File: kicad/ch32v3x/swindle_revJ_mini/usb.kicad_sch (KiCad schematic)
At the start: 8 parts, among them J4 USB, U2 LM1117-3.3

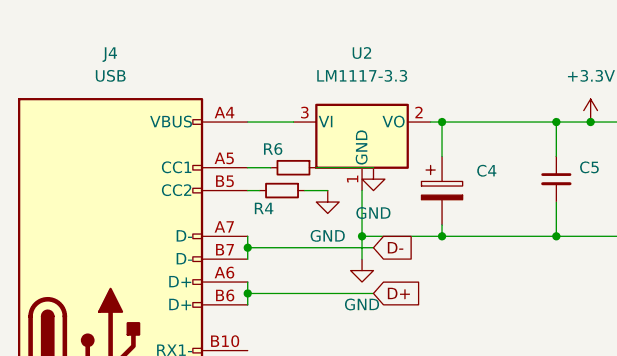
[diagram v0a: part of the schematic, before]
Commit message: add a WS2812b to the mini version, mini version for CH32,GD32 and RP2xxx
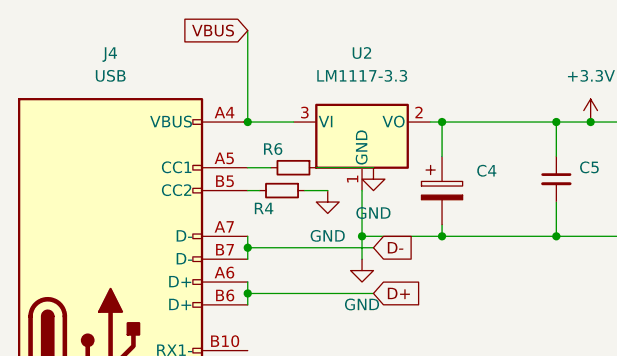
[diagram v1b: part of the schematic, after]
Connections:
- net VBUS: now reaches J4.A4 (VBUS), J4.A9 (VBUS), J4.B4 (VBUS), J4.B9 (VBUS), U2.3 (VI)
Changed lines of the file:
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@@
+	)
+	(junction
+		(at 101.6 45.72)
+		(diameter 0)
+		(color 0 0 0 0)
 	)
 	(junction
@@
 		(pts
 			(xy 123.19 57.15) (xy 123.19 58.42)
+		)
+		(stroke
+			(width 0)
+			(type default)
+		)
+	)
+	(wire
+		(pts
+			(xy 101.6 35.56) (xy 101.6 45.72)
 		)
 		(stroke
@@
 				(hide yes)
 			)
+		)
+	)
+	(global_label "VBUS"
+		(shape input)
+		(at 101.6 35.56 180)
+		(fields_autoplaced yes)
+		(effects
+			(font
+				(size 1.27 1.27)
+			)
+			(justify right)
+		)
+		(property "Intersheetrefs" "${INTERSHEET_REFS}"
+			(at 93.7162 35.56 0)
+			(effects
+				(font
+					(size 1.27 1.27)
+				)
+				(justify right)
+				(hide yes)
+			)

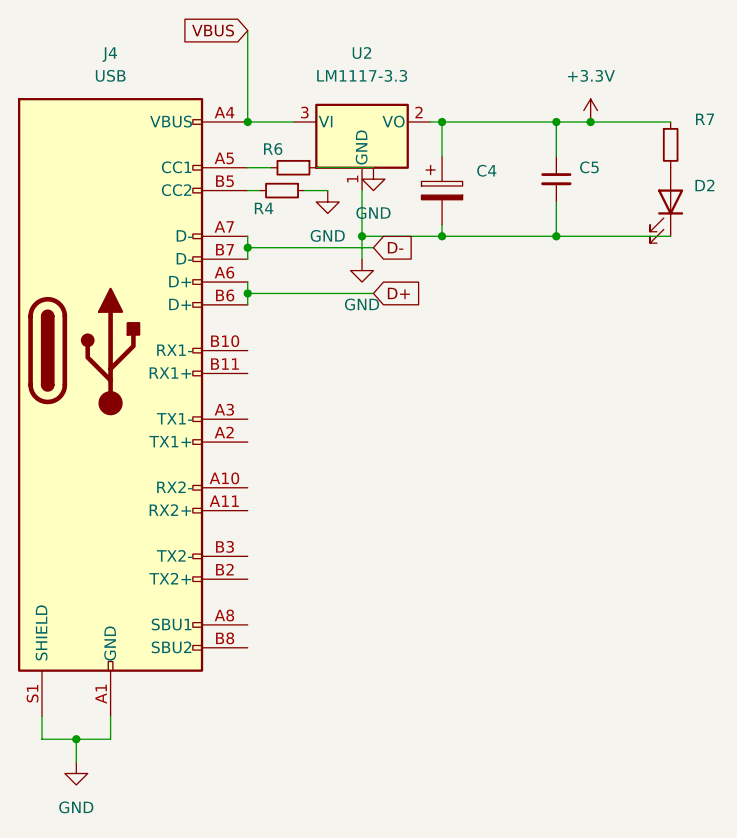
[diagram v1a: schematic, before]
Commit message: Kicad : ch32v3, add a (optional) 1.2k pullup on D+ so it can be used for GD32F303/64pins package
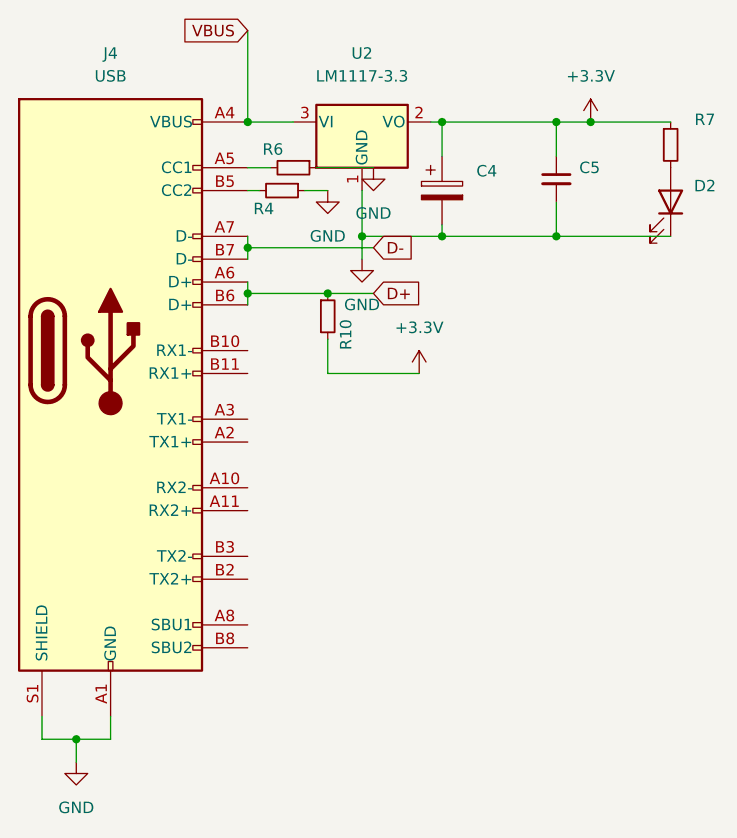
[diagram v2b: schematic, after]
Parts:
- added R10: 1.2k, Resistor_SMD:R_0603_1608Metric, symbol Device:R_Small
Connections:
- net +3.3V: now also R10.2
- net D+: now also R10.1
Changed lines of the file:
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@@
 		(color 0 0 0 0)
 	)
+	(junction
+		(at 110.49 64.77)
+		(diameter 0)
+		(color 0 0 0 0)
+	)
 	(wire
 		(pts
@@
 	(wire
 		(pts
+			(xy 110.49 64.77) (xy 115.57 64.77)
+		)
+		(stroke
+			(width 0)
+			(type default)
+		)
+	)
+	(wire
+		(pts
 			(xy 101.6 45.72) (xy 106.68 45.72)
 		)
@@
 	(wire
 		(pts
+			(xy 110.49 73.66) (xy 120.65 73.66)
+		)
+		(stroke
+			(width 0)
+			(type default)
+		)
+	)
+	(wire
+		(pts
 			(xy 78.74 114.3) (xy 82.55 114.3)
 		)
@@
 	(wire
 		(pts
+			(xy 110.49 69.85) (xy 110.49 73.66)
+		)
+		(stroke
+			(width 0)
+			(type default)
+		)
+	)
+	(wire
+		(pts
 			(xy 135.89 49.53) (xy 135.89 45.72)
 		)
@@
 	(wire
 		(pts
-			(xy 101.6 64.77) (xy 115.57 64.77)
+			(xy 101.6 64.77) (xy 110.49 64.77)
 		)
 		(stroke
@@
 	)
 	(symbol
+		(lib_id "power:+3.3V")
+		(at 120.65 73.66 0)
+		(mirror y)
+		(unit 1)
+		(exclude_from_sim no)
+		(in_bom yes)
+		(on_board yes)
+		(dnp no)
+		(property "Reference" "#PWR023"
+			(at 120.65 77.47 0)
+			(effects
+				(font
+					(size 1.27 1.27)
+				)
+				(hide yes)
+			)
+		)
+		(property "Value" "+3.3V"
+			(at 120.65 68.58 0)
+			(effects
+				(font
+					(size 1.27 1.27)
+				)
+			)
+		)
+		(property "Footprint" ""
+			(at 120.65 73.66 0)
+			(effects
+				(font
+					(size 1.27 1.27)
+				)
+				(hide yes)
+			)
+		)
+		(property "Datasheet" ""
+			(at 120.65 73.66 0)
+			(effects
+				(font
+					(size 1.27 1.27)
+				)
+				(hide yes)
+			)
+		)
+		(property "Description" ""
+			(at 120.65 73.66 0)
+			(effects
+				(font
+					(size 1.27 1.27)
+				)
+				(hide yes)
+			)
+		)
+		(pin "1"
+		)
+		(instances
+			(project "swindle_ch32_revJ_mini"
+				(path "/fbe443d6-6d74-4abc-9dee-16e0160553bc/9ae6e029-7457-493b-8bae-ed725714055d"
+					(reference "#PWR023")
+					(unit 1)
+				)
+			)
+		)
+	)
+	(symbol
 		(lib_id "Device:C_Polarized")
 		(at 123.19 53.34 0)
@@
 					(unit 1)
 				)
+			)
+		)
+	)
+	(symbol
+		(lib_id "Device:R_Small")
+		(at 110.49 67.31 0)
+		(unit 1)
+		(exclude_from_sim no)
+		(in_bom yes)
+		(on_board yes)
+		(dnp no)
+		(property "Reference" "R10"
+			(at 112.522 69.342 90)
+			(effects
+				(font
+					(size 1.27 1.27)
+				)
+			)
+		)
+		(property "Value" "1.2k"
+			(at 112.522 65.786 90)
+			(effects
+				(font
+					(size 1.27 1.27)
+				)
+				(hide yes)
+			)
+		)
+		(property "Footprint" "Resistor_SMD:R_0603_1608Metric"
+			(at 110.49 67.31 0)
+			(effects
+				(font
+					(size 1.27 1.27)
+				)
+				(hide yes)
+			)
+		)
+		(property "Datasheet" "~"
+			(at 110.49 67.31 0)
+			(effects
+				(font
+					(size 1.27 1.27)
+				)
+				(hide yes)
+			)
+		)
+		(property "Description" ""
+			(at 110.49 67.31 0)
+			(effects
+				(font
+					(size 1.27 1.27)
+				)
+				(hide yes)
+			)
+		)
+		(pin "1"
+		)
+		(pin "2"
+		)
+		(instances
+			(project "swindle_ch32_revJ_mini"
+				(path "/fbe443d6-6d74-4abc-9dee-16e0160553bc/9ae6e029-7457-493b-8bae-ed725714055d"
+					(reference "R10")
+					(unit 1)
+				)
